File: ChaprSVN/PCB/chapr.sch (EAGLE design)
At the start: 28 parts, among them M2 RN42 Module, T1 3906, T2 3904

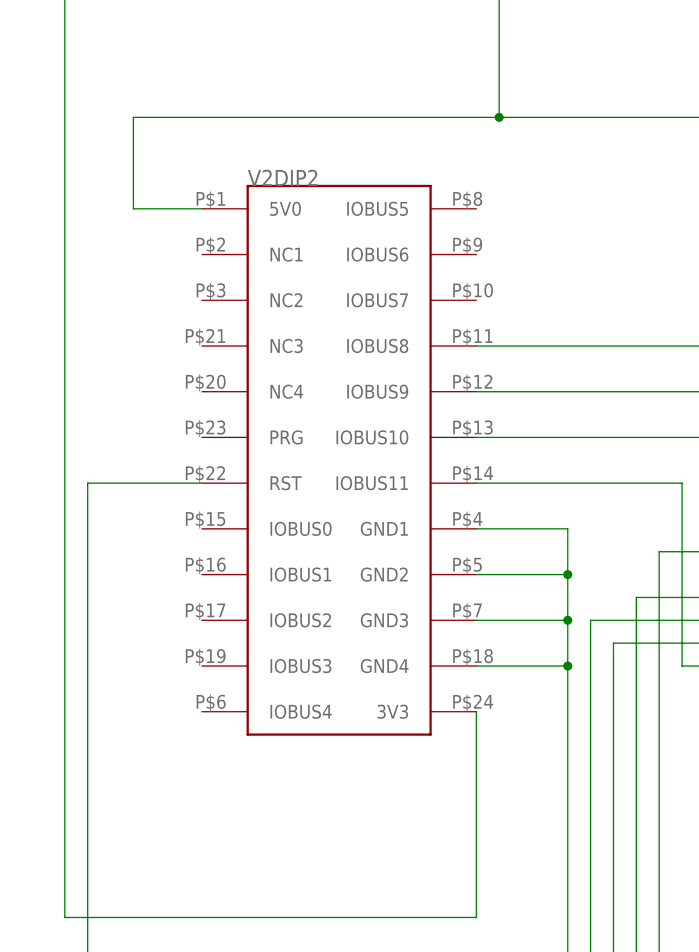
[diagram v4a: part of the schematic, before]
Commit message: 
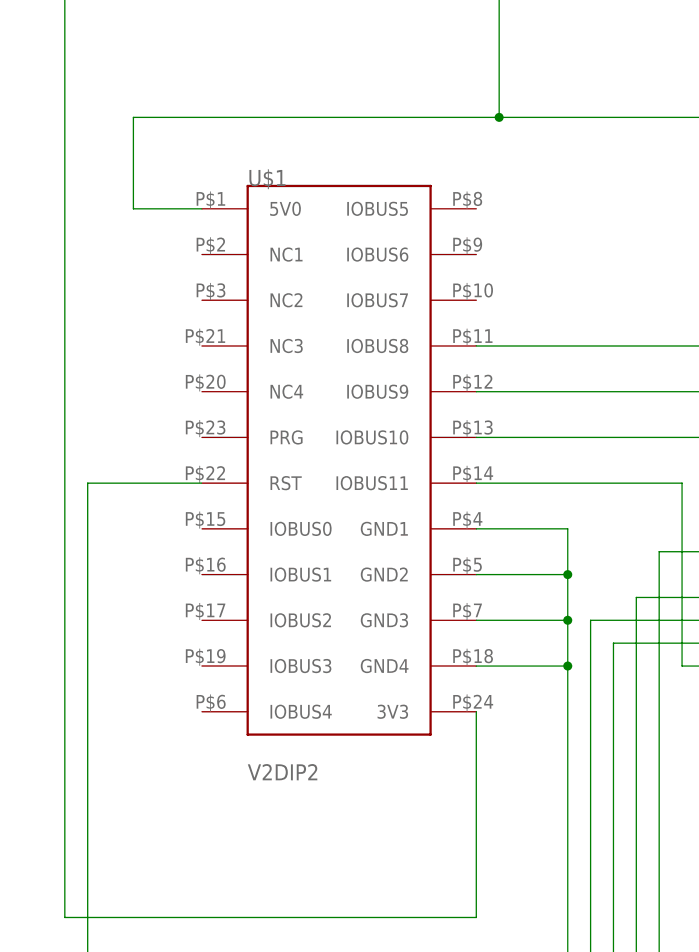
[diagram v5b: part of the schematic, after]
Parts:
- renumbered V2DIP2 to U$1
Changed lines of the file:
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@@
 <part name="R17" library="resistor" deviceset="R-US_" device="0207/10" value="24K"/>
 <part name="R16" library="resistor" deviceset="R-US_" device="0207/10" value="24K"/>
-<part name="V2DIP2" library="ChapR-Custom" deviceset="V2DIP2" device=""/>
+<part name="U$1" library="ChapR-Custom" deviceset="V2DIP2" device=""/>
 </parts>
 <sheets>
@@
 <attribute name="VALUE" x="37.338" y="-26.67" size="1.778" layer="96" rot="R270"/>
 </instance>
-<instance part="V2DIP2" gate="G$1" x="-60.96" y="71.12" smashed="yes">
-<attribute name="NAME" x="-71.12" y="101.6" size="1.778" layer="95"/>
-</instance>
+<instance part="U$1" gate="G$1" x="-60.96" y="71.12"/>
 </instances>
 <busses>
@@
 </segment>
 <segment>
-<pinref part="V2DIP2" gate="G$1" pin="GND1"/>
 <wire x1="-45.72" y1="63.5" x2="-35.56" y2="63.5" width="0.1524" layer="91"/>
 <wire x1="-35.56" y1="63.5" x2="-35.56" y2="58.42" width="0.1524" layer="91"/>
 <pinref part="GND1" gate="1" pin="GND"/>
-<pinref part="V2DIP2" gate="G$1" pin="GND2"/>
 <wire x1="-35.56" y1="58.42" x2="-35.56" y2="53.34" width="0.1524" layer="91"/>
 <wire x1="-35.56" y1="53.34" x2="-35.56" y2="48.26" width="0.1524" layer="91"/>
 <wire x1="-35.56" y1="48.26" x2="-35.56" y2="12.7" width="0.1524" layer="91"/>
 <wire x1="-45.72" y1="58.42" x2="-35.56" y2="58.42" width="0.1524" layer="91"/>
-<pinref part="V2DIP2" gate="G$1" pin="GND3"/>
 <wire x1="-45.72" y1="53.34" x2="-35.56" y2="53.34" width="0.1524" layer="91"/>
 <junction x="-35.56" y="53.34"/>
 <junction x="-35.56" y="58.42"/>
-<pinref part="V2DIP2" gate="G$1" pin="GND4"/>
 <wire x1="-45.72" y1="48.26" x2="-35.56" y2="48.26" width="0.1524" layer="91"/>
 <junction x="-35.56" y="48.26"/>
+<pinref part="U$1" gate="G$1" pin="GND4"/>
+<pinref part="U$1" gate="G$1" pin="GND3"/>
+<pinref part="U$1" gate="G$1" pin="GND2"/>
+<pinref part="U$1" gate="G$1" pin="GND1"/>
 </segment>
 </net>
@@
 <wire x1="-91.44" y1="129.54" x2="-91.44" y2="20.32" width="0.1524" layer="91"/>
 <wire x1="-91.44" y1="20.32" x2="-45.72" y2="20.32" width="0.1524" layer="91"/>
-<pinref part="V2DIP2" gate="G$1" pin="3V3"/>
 <wire x1="-45.72" y1="20.32" x2="-45.72" y2="43.18" width="0.1524" layer="91"/>
+<pinref part="U$1" gate="G$1" pin="3V3"/>
 </segment>
 </net>
@@
 <pinref part="P+1" gate="1" pin="+5V"/>
 <wire x1="-83.82" y1="109.22" x2="-83.82" y2="99.06" width="0.1524" layer="91"/>
-<pinref part="V2DIP2" gate="G$1" pin="5V0"/>
 <wire x1="-83.82" y1="99.06" x2="-76.2" y2="99.06" width="0.1524" layer="91"/>
+<pinref part="U$1" gate="G$1" pin="5V0"/>
 </segment>
 </net>
@@
 <wire x1="15.24" y1="15.24" x2="-88.9" y2="15.24" width="0.1524" layer="91"/>
 <wire x1="-88.9" y1="15.24" x2="-88.9" y2="68.58" width="0.1524" layer="91"/>
-<pinref part="V2DIP2" gate="G$1" pin="RST"/>
 <wire x1="-88.9" y1="68.58" x2="-76.2" y2="68.58" width="0.1524" layer="91"/>
+<pinref part="U$1" gate="G$1" pin="RST"/>
 </segment>
 </net>
 <net name="N$10" class="0">
 <segment>
-<pinref part="V2DIP2" gate="G$1" pin="IOBUS11"/>
 <wire x1="-45.72" y1="68.58" x2="-22.86" y2="68.58" width="0.1524" layer="91"/>
 <wire x1="-22.86" y1="68.58" x2="-22.86" y2="48.26" width="0.1524" layer="91"/>
 <pinref part="ARDUINO" gate="G$1" pin="D6"/>
 <wire x1="-22.86" y1="48.26" x2="-12.7" y2="48.26" width="0.1524" layer="91"/>
+<pinref part="U$1" gate="G$1" pin="IOBUS11"/>
 </segment>
 </net>
 <net name="N$11" class="0">
 <segment>
-<pinref part="V2DIP2" gate="G$1" pin="IOBUS10"/>
 <wire x1="-45.72" y1="73.66" x2="-20.32" y2="73.66" width="0.1524" layer="91"/>
 <wire x1="-20.32" y1="73.66" x2="-20.32" y2="45.72" width="0.1524" layer="91"/>
 <pinref part="ARDUINO" gate="G$1" pin="D7"/>
 <wire x1="-20.32" y1="45.72" x2="-12.7" y2="45.72" width="0.1524" layer="91"/>
+<pinref part="U$1" gate="G$1" pin="IOBUS10"/>
 </segment>
 </net>
 <net name="N$12" class="0">
 <segment>
-<pinref part="V2DIP2" gate="G$1" pin="IOBUS9"/>
 <wire x1="-45.72" y1="78.74" x2="-17.78" y2="78.74" width="0.1524" layer="91"/>
 <wire x1="-17.78" y1="78.74" x2="-17.78" y2="43.18" width="0.1524" layer="91"/>
 <pinref part="ARDUINO" gate="G$1" pin="D8"/>
 <wire x1="-17.78" y1="43.18" x2="-12.7" y2="43.18" width="0.1524" layer="91"/>
+<pinref part="U$1" gate="G$1" pin="IOBUS9"/>
 </segment>
 </net>
 <net name="N$13" class="0">
 <segment>
-<pinref part="V2DIP2" gate="G$1" pin="IOBUS8"/>
 <wire x1="-45.72" y1="83.82" x2="-15.24" y2="83.82" width="0.1524" layer="91"/>
 <wire x1="-15.24" y1="83.82" x2="-15.24" y2="40.64" width="0.1524" layer="91"/>
 <pinref part="ARDUINO" gate="G$1" pin="D9"/>
 <wire x1="-15.24" y1="40.64" x2="-12.7" y2="40.64" width="0.1524" layer="91"/>
-</segment>
-</net>
+<pinref part="U$1" gate="G$1" pin="IOBUS8"/>
+</segment>
+</net>
